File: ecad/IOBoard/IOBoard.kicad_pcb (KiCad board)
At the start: 2 copper layers, 9 parts, among them J1 SN37A12A, J3 toEffectsBoard, J4 SN37A12A, U1 FS57003PLT2B2M2QE

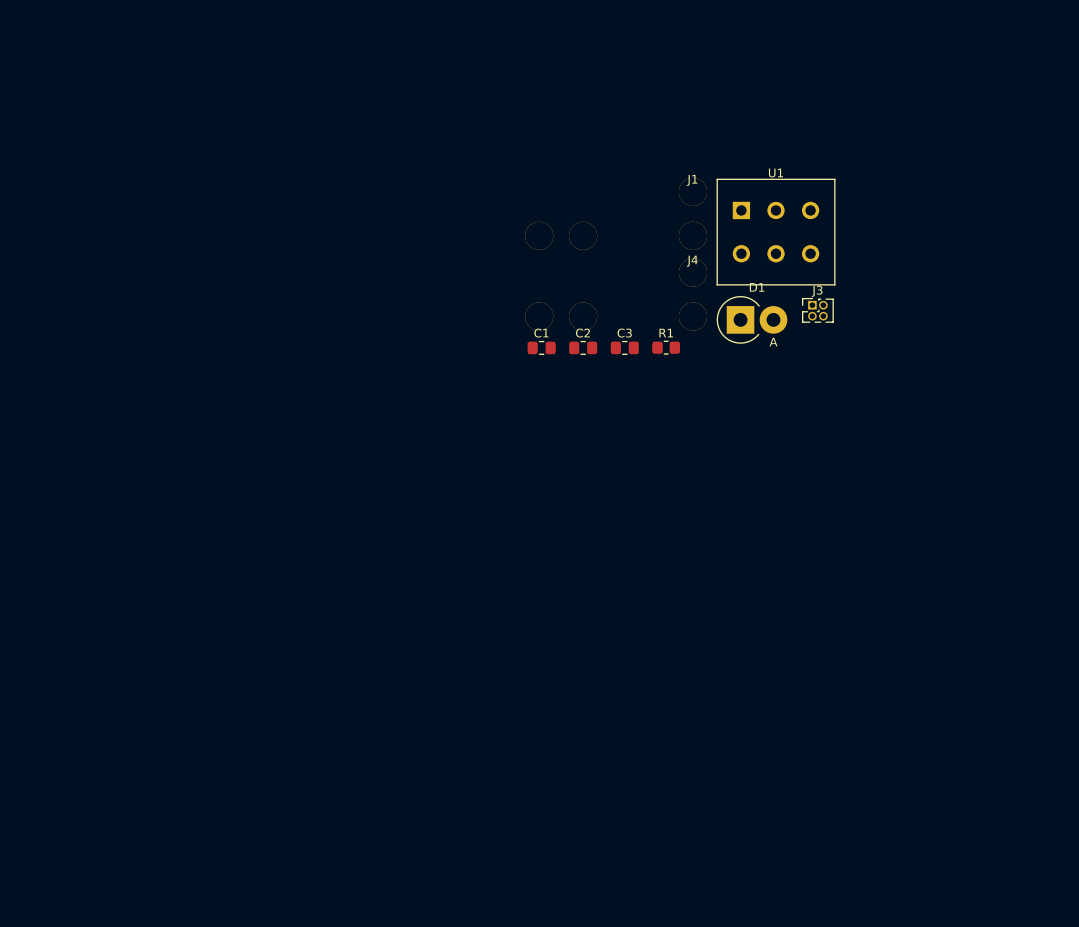
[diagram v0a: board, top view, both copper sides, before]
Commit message: Update libraries and CAD
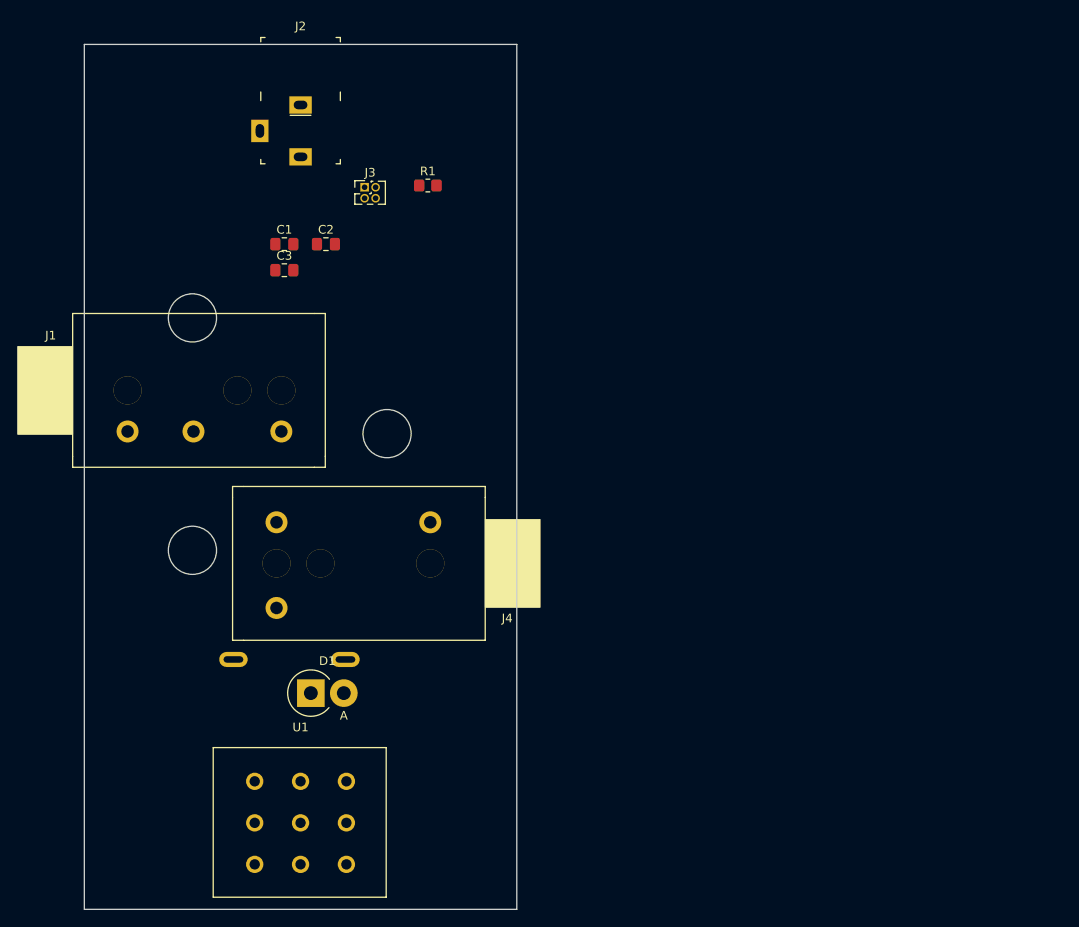
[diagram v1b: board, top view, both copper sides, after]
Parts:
- added BAT1: BC9VPC, DigiKey:Battery_Holder_9V_BC9VPC-ND, B.Cu at (62.5, 108.5)
- added J2: PJ-102A, DigiKey:Barrel_Jack_5.5mmODx2.1mmID_PJ-102A, F.Cu at (75.0, 60.0)
- J1: value SN37A12A -> SN37A12B; footprint screaming-panda:SN37A -> screaming-panda:Switchcraft_SN37A12B
- J4: footprint screaming-panda:SN37A -> screaming-panda:Switchcraft_SN37A12A
- U1: footprint Button_Switch_THT:SW_PUSH_E-Switch_FS5700DP_DPDT -> screaming-panda:SW_PUSH_E-Switch_FS57003PLT_3PDT
- moved U1 87.2 mm to (75.0, 140.0)
- moved J1 67.8 mm to (55.0, 90.0), turned to 180 degrees
- moved D1 65.8 mm to (76.2, 125.0)
- moved J3 53.5 mm to (82.4, 66.5)
- moved J4 41.7 mm to (90.0, 110.0)
- moved C3 40.4 mm to (73.1, 76.1)
- moved R1 33.3 mm to (89.7, 66.3)
- moved C1 32.1 mm to (73.1, 73.1)
- moved C2 32.1 mm to (77.9, 73.1)
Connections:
- U1 pad 1: /SIG_IN -> Net-(D1-Pad1)
- U1 pad 2: /SIG_IN -> GND
- U1 pad 4: Net-(D1-Pad1) -> /SIG_IN
- U1 pad 5: GND -> /SIG_IN
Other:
- board outline added: 50 x 100 mm

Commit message: Route IOBoard
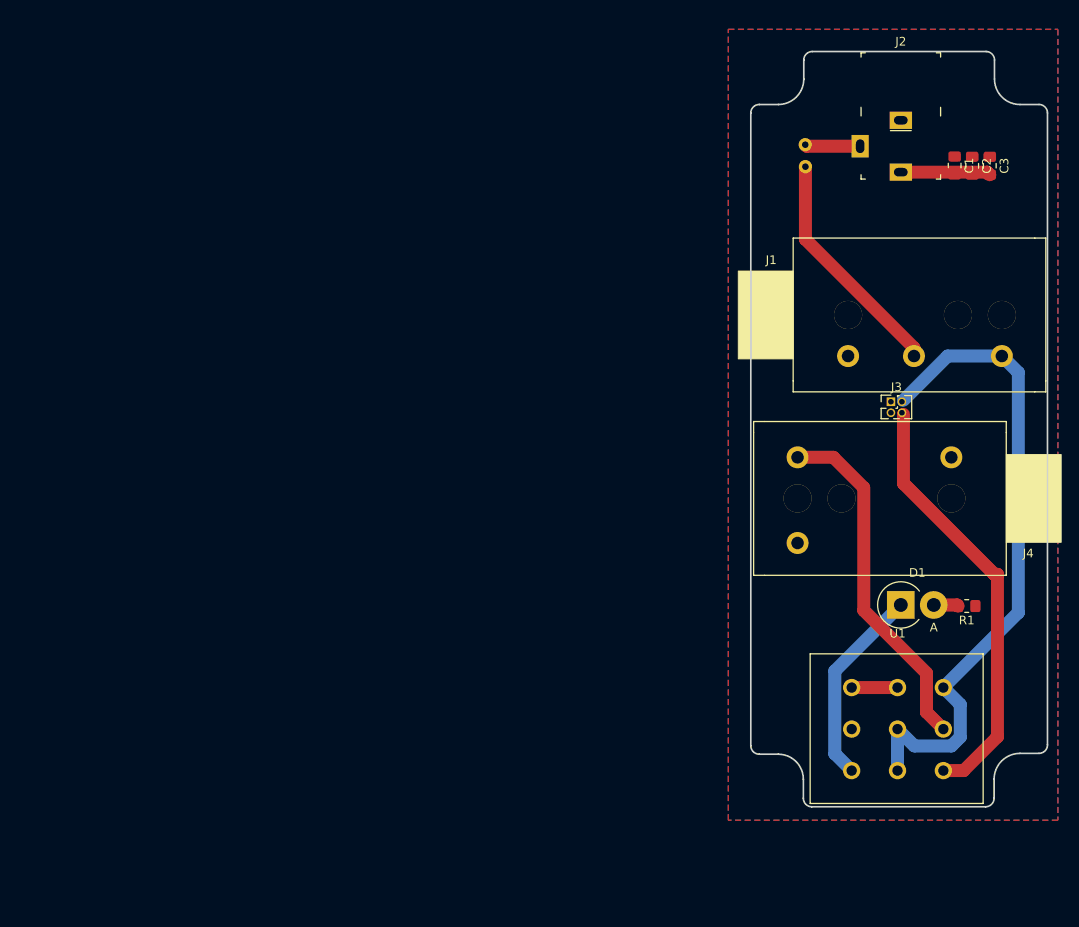
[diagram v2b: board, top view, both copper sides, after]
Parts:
- BAT1: footprint DigiKey:Battery_Holder_9V_BC9VPC-ND -> DigiKey:PinHeader_1x2_P2.54mm
- moved BAT1 85.0 mm to (133.3, 61.6)
- moved J1 83.8 mm to (138.3, 81.3)
- moved C3 82.5 mm to (154.7, 64.0), turned to 270 degrees
- moved R1 79.0 mm to (152.0, 114.9), turned to 180 degrees
- moved C1 78.0 mm to (150.6, 64.0), turned to 270 degrees
- moved C2 75.3 mm to (152.7, 64.0), turned to 270 degrees
- moved U1 69.9 mm to (144.0, 129.2)
- moved J2 69.4 mm to (144.4, 61.8)
- moved D1 69.0 mm to (144.4, 114.8)
- moved J3 65.7 mm to (143.3, 91.3)
- moved J4 60.7 mm to (150.2, 102.5)
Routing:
- net /SIG_IN: track 0.00 -> 83.4 mm
- net /EFFECT_OUT: track 0.00 -> 73.1 mm
- net /SIG_OUT: track 0.00 -> 40.8 mm
- net Net-(BAT1-PadNEG): track 0.00 -> 27.1 mm
- net Net-(D1-Pad1): track 0.00 -> 23.1 mm
- net GND: track 0.00 -> 10.4 mm
- net Net-(BAT1-PadPOS): track 0.00 -> 6.42 mm
- net Net-(U1-Pad3): track 0.00 -> 5.30 mm
- net Net-(D1-Pad2): track 0.00 -> 2.86 mm
- added copper zone on F.Cu, net +9V
- added copper zone on B.Cu, net GND
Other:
- board size 50 x 100 mm -> 34.3 x 87.3 mm

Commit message: Add barrel jack 3D step
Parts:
- J2: footprint DigiKey:Barrel_Jack_5.5mmODx2.1mmID_PJ-102A -> screaming-panda:Barrel_Jack_5.5mmODx2.1mmID_PJ-102A
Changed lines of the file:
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@@
   )
   (setup
-    (last_trace_width 1.5)
+    (last_trace_width 0.25)
     (user_trace_width 0.75)
     (user_trace_width 1)
@@
     (add_net "Net-(U1-Pad3)")
   )
+  (module screaming-panda:Barrel_Jack_5.5mmODx2.1mmID_PJ-102A (layer F.Cu)
+    (at 144.399 61.77)
+    (fp_text reference J2 (at 5.601 -6.77 90) (layer F.SilkS)
+      (effects (font (size 1 1) (thickness 0.15)))
+    )
+    (fp_text value PJ-102A (at 0 5.8) (layer F.Fab)
+      (effects (font (size 1 1) (thickness 0.15)))
+    )
+    (fp_line (start -4.5 3.7) (end 4.5 3.7) (layer F.Fab) (width 0.1))
+    (fp_line (start -4.5 3.7) (end -4.5 -10.7) (layer F.Fab) (width 0.1))
+    (fp_line (start 4.5 3.7) (end 4.5 -10.7) (layer F.Fab) (width 0.1))
+    (fp_line (start -4.5 -10.7) (end 4.5 -10.7) (layer F.Fab) (width 0.1))
+    (fp_line (start 4.6 3.8) (end 4.1 3.8) (layer F.SilkS) (width 0.1))
+    (fp_line (start 4.6 3.8) (end 4.6 3.3) (layer F.SilkS) (width 0.1))
+    (fp_line (start -4.6 3.8) (end -4.1 3.8) (layer F.SilkS) (width 0.1))
+    (fp_line (start -4.6 3.8) (end -4.6 3.3) (layer F.SilkS) (width 0.1))
+    (fp_line (start -1.2 -1.8) (end 1.2 -1.8) (layer F.SilkS) (width 0.1))
+    (fp_line (start -4.6 -10.8) (end -4.6 -10.3) (layer F.SilkS) (width 0.1))
+    (fp_line (start -4.6 -10.8) (end -4.1 -10.8) (layer F.SilkS) (width 0.1))
+    (fp_line (start 4.6 -10.8) (end 4.1 -10.8) (layer F.SilkS) (width 0.1))
+    (fp_line (start 4.6 -10.8) (end 4.6 -10.3) (layer F.SilkS) (width 0.1))
+    (fp_line (start -4.6 -3.5) (end -4.6 -4.5) (layer F.SilkS) (width 0.1))
+    (fp_line (start 4.6 -3.5) (end 4.6 -4.5) (layer F.SilkS) (width 0.1))
+    (fp_line (start -5.9 -10.95) (end 4.8 -10.95) (layer F.CrtYd) (width 0.05))
+    (fp_line (start -5.9 -10.95) (end -5.9 4.25) (layer F.CrtYd) (width 0.05))
+    (fp_line (start 4.8 -10.95) (end 4.8 4.25) (layer F.CrtYd) (width 0.05))
+    (fp_line (start -5.9 4.25) (end 4.8 4.25) (layer F.CrtYd) (width 0.05))
+    (pad 2 thru_hole rect (at 0 -3) (size 2.6 2) (drill oval 1.6 1) (layers *.Cu *.Mask)
+      (net 2 +9V))
+    (pad 1 thru_hole rect (at 0 3) (size 2.6 2) (drill oval 1.6 1) (layers *.Cu *.Mask)
+      (net 1 GND))
+    (pad 3 thru_hole rect (at -4.7 0) (size 2 2.6) (drill oval 1 1.6) (layers *.Cu *.Mask)
+      (net 7 "Net-(BAT1-PadPOS)"))
+    (model :CAD:screaming-panda/mcad/step_imports/CUI_DEVICES_PJ-102A.step
+      (offset (xyz -0.1016 10.6426 5.6388))
+      (scale (xyz 1 1 1))
+      (rotate (xyz -90 0 -90))
+    )
+  )
   (module DigiKey:PinHeader_1x2_P2.54mm (layer B.Cu)
     (at 133.35 61.595 270)
@@
     )
     (fp_text value BC9VPC (at 1.26 -2.84 90) (layer B.Fab)
-      (effects (font (size 1 1) (thickness 0.15)) (justify mirror))
-    )
-    (fp_text user %R (at 1.2 0 90) (layer B.Fab)
       (effects (font (size 1 1) (thickness 0.15)) (justify mirror))
     )
@@
     (fp_line (start -1.27 1.27) (end 3.81 1.27) (layer B.Fab) (width 0.1))
     (fp_line (start -1.27 -1.27) (end -1.27 1.27) (layer B.Fab) (width 0.1))
+    (fp_text user %R (at 1.2 0 90) (layer B.Fab)
+      (effects (font (size 1 1) (thickness 0.15)) (justify mirror))
+    )
     (pad NEG thru_hole circle (at 2.54 -0.02 270) (size 1.524 1.524) (drill 0.762) (layers *.Cu *.Mask)
       (net 8 "Net-(BAT1-PadNEG)"))
@@
     )
   )
-  (module DigiKey:Barrel_Jack_5.5mmODx2.1mmID_PJ-102A (layer F.Cu)
-    (at 144.399 61.77)
-    (fp_text reference J2 (at 0 -12.1) (layer F.SilkS)
-      (effects (font (size 1 1) (thickness 0.15)))
-    )
-    (fp_text value PJ-102A (at -6.604 6.81 90) (layer F.Fab)
-      (effects (font (size 1 1) (thickness 0.15)))
-    )
-    (fp_line (start -5.9 4.25) (end 4.8 4.25) (layer F.CrtYd) (width 0.05))
-    (fp_line (start 4.8 -10.95) (end 4.8 4.25) (layer F.CrtYd) (width 0.05))
-    (fp_line (start -5.9 -10.95) (end -5.9 4.25) (layer F.CrtYd) (width 0.05))
-    (fp_line (start -5.9 -10.95) (end 4.8 -10.95) (layer F.CrtYd) (width 0.05))
-    (fp_line (start 4.6 -3.5) (end 4.6 -4.5) (layer F.SilkS) (width 0.1))
-    (fp_line (start -4.6 -3.5) (end -4.6 -4.5) (layer F.SilkS) (width 0.1))
-    (fp_line (start 4.6 -10.8) (end 4.6 -10.3) (layer F.SilkS) (width 0.1))
-    (fp_line (start 4.6 -10.8) (end 4.1 -10.8) (layer F.SilkS) (width 0.1))
-    (fp_line (start -4.6 -10.8) (end -4.1 -10.8) (layer F.SilkS) (width 0.1))
-    (fp_line (start -4.6 -10.8) (end -4.6 -10.3) (layer F.SilkS) (width 0.1))
-    (fp_line (start -1.2 -1.8) (end 1.2 -1.8) (layer F.SilkS) (width 0.1))
-    (fp_line (start -4.6 3.8) (end -4.6 3.3) (layer F.SilkS) (width 0.1))
-    (fp_line (start -4.6 3.8) (end -4.1 3.8) (layer F.SilkS) (width 0.1))
-    (fp_line (start 4.6 3.8) (end 4.6 3.3) (layer F.SilkS) (width 0.1))
-    (fp_line (start 4.6 3.8) (end 4.1 3.8) (layer F.SilkS) (width 0.1))
-    (fp_line (start -4.5 -10.7) (end 4.5 -10.7) (layer F.Fab) (width 0.1))
-    (fp_line (start 4.5 3.7) (end 4.5 -10.7) (layer F.Fab) (width 0.1))
-    (fp_line (start -4.5 3.7) (end -4.5 -10.7) (layer F.Fab) (width 0.1))
-    (fp_line (start -4.5 3.7) (end 4.5 3.7) (layer F.Fab) (width 0.1))
-    (pad 2 thru_hole rect (at 0 -3) (size 2.6 2) (drill oval 1.6 1) (layers *.Cu *.Mask)
-      (net 2 +9V))
-    (pad 1 thru_hole rect (at 0 3) (size 2.6 2) (drill oval 1.6 1) (layers *.Cu *.Mask)
-      (net 1 GND))
-    (pad 3 thru_hole rect (at -4.7 0) (size 2 2.6) (drill oval 1 1.6) (layers *.Cu *.Mask)
-      (net 7 "Net-(BAT1-PadPOS)"))
-  )
   (module screaming-panda:Switchcraft_SN37A12B (layer F.Cu)
     (at 138.303 81.28 180)
@@
       (effects (font (size 1 1) (thickness 0.15)))
     )
-    (fp_text user A (at 3.81 2.6) (layer F.SilkS)
-      (effects (font (size 1 1) (thickness 0.15)))
-    )
-    (fp_text user A (at 3.81 2.6) (layer F.Fab)
-      (effects (font (size 1 1) (thickness 0.15)))
-    )
-    (fp_text user %R (at 1.905 -3.72) (layer F.Fab)
-      (effects (font (size 1 1) (thickness 0.15)))
-    )
-    (fp_arc (start 0 0) (end 2.154716 -1.6) (angle -284.776236) (layer F.SilkS) (width 0.12))
     (fp_circle (center 0 0) (end 2.6 0) (layer F.Fab) (width 0.1))
     (fp_line (start 0 0) (end 3.81 0) (layer F.Fab) (width 0.1))
@@
     (fp_line (start 5.66 2.85) (end 5.66 -2.85) (layer F.CrtYd) (width 0.05))
     (fp_line (start 5.66 -2.85) (end -2.85 -2.85) (layer F.CrtYd) (width 0.05))
+    (fp_text user A (at 3.81 2.6) (layer F.SilkS)
+      (effects (font (size 1 1) (thickness 0.15)))
+    )
+    (fp_text user A (at 3.81 2.6) (layer F.Fab)
+      (effects (font (size 1 1) (thickness 0.15)))
+    )
+    (fp_text user %R (at 1.905 -3.72) (layer F.Fab)
+      (effects (font (size 1 1) (thickness 0.15)))
+    )
+    (fp_arc (start 0 0) (end 2.154716 -1.6) (angle -284.776236) (layer F.SilkS) (width 0.12))
     (pad 2 thru_hole oval (at 3.81 0) (size 3.2 3.2) (drill 1.6) (layers *.Cu *.Mask)
       (net 3 "Net-(D1-Pad2)"))
@@
     (tags "capacitor handsolder")
     (attr smd)
-    (fp_text reference C3 (at 0 -1.68 90) (layer F.SilkS)
+    (fp_text reference C3 (at -3.5295 0.186 270) (layer F.SilkS)
       (effects (font (size 1 1) (thickness 0.15)))
     )
     (fp_text value 10n (at 0 1.68 90) (layer F.Fab)
       (effects (font (size 1 1) (thickness 0.15)))
-    )
-    (fp_text user %R (at 0 0 90) (layer F.Fab)
-      (effects (font (size 0.5 0.5) (thickness 0.08)))
     )
     (fp_line (start -1 0.625) (end -1 -0.625) (layer F.Fab) (width 0.1))
@@
     (fp_line (start 1.88 -0.98) (end 1.88 0.98) (layer F.CrtYd) (width 0.05))
     (fp_line (start 1.88 0.98) (end -1.88 0.98) (layer F.CrtYd) (width 0.05))
+    (fp_text user %R (at 0 0 90) (layer F.Fab)
+      (effects (font (size 0.5 0.5) (thickness 0.08)))
+    )
     (pad 2 smd roundrect (at 1.0375 0 270) (size 1.175 1.45) (layers F.Cu F.Paste F.Mask) (roundrect_rratio 0.212766)
       (net 1 GND))
@@
     (tags "capacitor handsolder")
     (attr smd)
-    (fp_text reference C2 (at 0 -1.68 90) (layer F.SilkS)
+    (fp_text reference C2 (at -3.5295 0.154 90) (layer F.SilkS)
       (effects (font (size 1 1) (thickness 0.15)))
     )
     (fp_text value 1u (at 0 1.68 90) (layer F.Fab)
       (effects (font (size 1 1) (thickness 0.15)))
-    )
-    (fp_text user %R (at 0 0 90) (layer F.Fab)
-      (effects (font (size 0.5 0.5) (thickness 0.08)))
     )
     (fp_line (start -1 0.625) (end -1 -0.625) (layer F.Fab) (width 0.1))
@@
     (fp_line (start 1.88 -0.98) (end 1.88 0.98) (layer F.CrtYd) (width 0.05))
     (fp_line (start 1.88 0.98) (end -1.88 0.98) (layer F.CrtYd) (width 0.05))
+    (fp_text user %R (at 0 0 90) (layer F.Fab)
+      (effects (font (size 0.5 0.5) (thickness 0.08)))
+    )
     (pad 2 smd roundrect (at 1.0375 0 270) (size 1.175 1.45) (layers F.Cu F.Paste F.Mask) (roundrect_rratio 0.212766)
       (net 1 GND))
@@
     (tags "capacitor handsolder")
     (attr smd)
-    (fp_text reference C1 (at 0 -1.68 90) (layer F.SilkS)
+    (fp_text reference C1 (at -3.508 0.122 90) (layer F.SilkS)
       (effects (font (size 1 1) (thickness 0.15)))
     )
     (fp_text value 100u (at 0 1.68 90) (layer F.Fab)
       (effects (font (size 1 1) (thickness 0.15)))
-    )
-    (fp_text user %R (at 0 0 90) (layer F.Fab)
-      (effects (font (size 0.5 0.5) (thickness 0.08)))
     )
     (fp_line (start -1 0.625) (end -1 -0.625) (layer F.Fab) (width 0.1))
@@
     (fp_line (start 1.88 -0.98) (end 1.88 0.98) (layer F.CrtYd) (width 0.05))
     (fp_line (start 1.88 0.98) (end -1.88 0.98) (layer F.CrtYd) (width 0.05))
+    (fp_text user %R (at 0 0 90) (layer F.Fab)
+      (effects (font (size 0.5 0.5) (thickness 0.08)))
+    )
     (pad 2 smd roundrect (at 1.0375 0 270) (size 1.175 1.45) (layers F.Cu F.Paste F.Mask) (roundrect_rratio 0.212766)
       (net 1 GND))
